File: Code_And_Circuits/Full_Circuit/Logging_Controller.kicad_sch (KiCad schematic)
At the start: 4 parts, among them J1 Micro_SD_Card_Slot, M1 GY-GPS6MV2

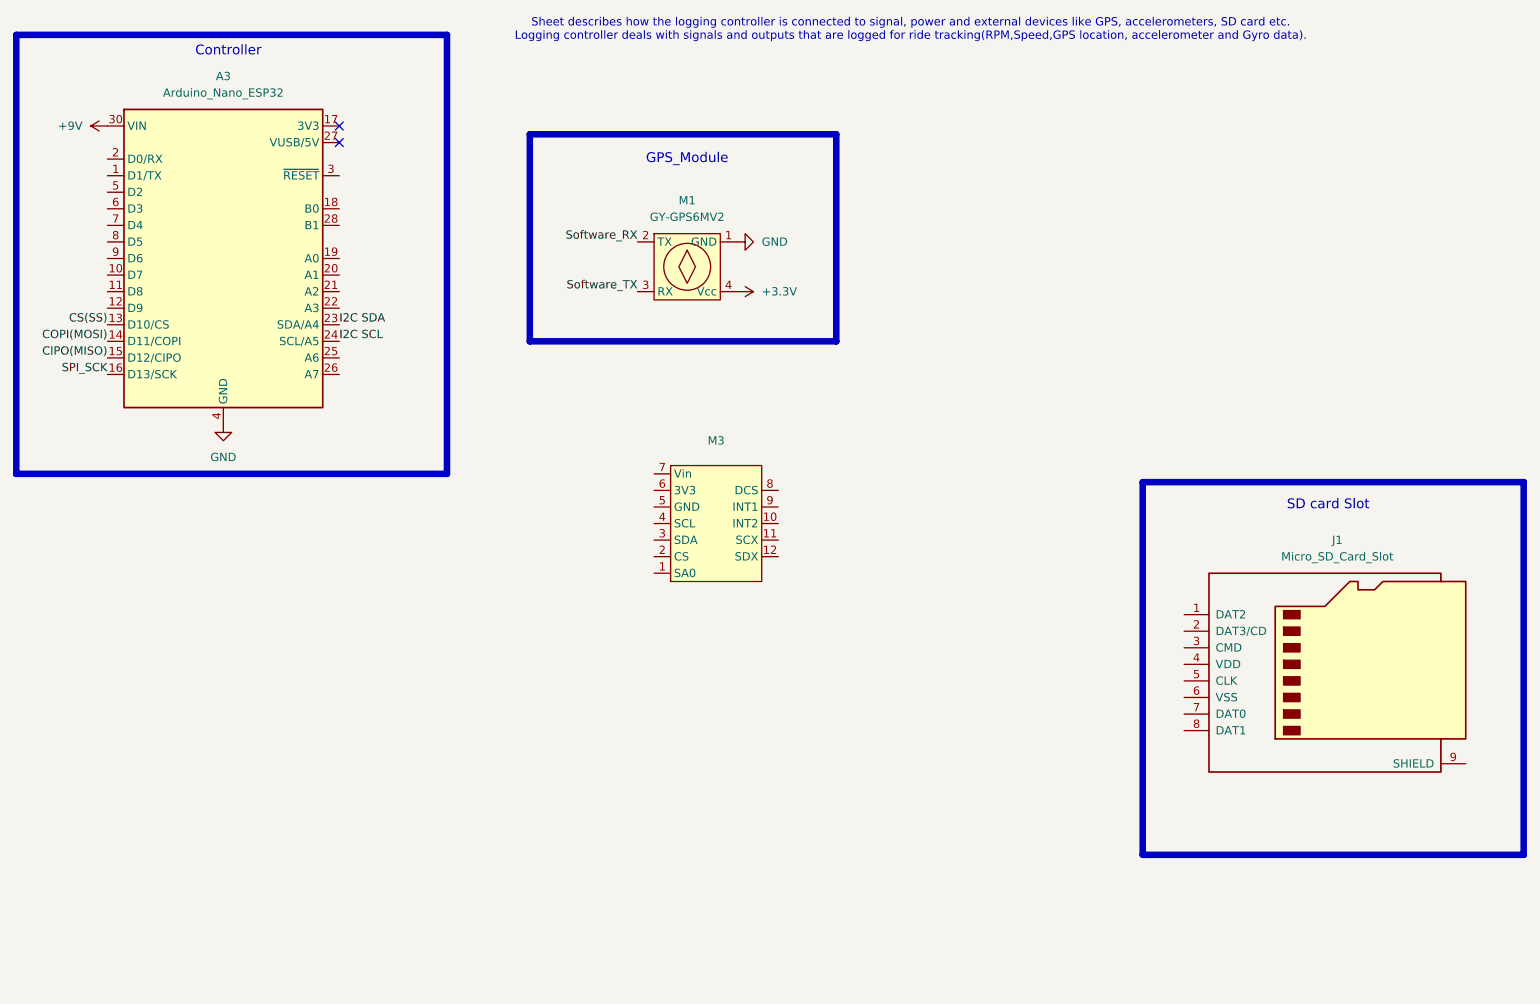
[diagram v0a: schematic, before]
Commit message: Finished schematic need to do PCB design and get Tachometer reference
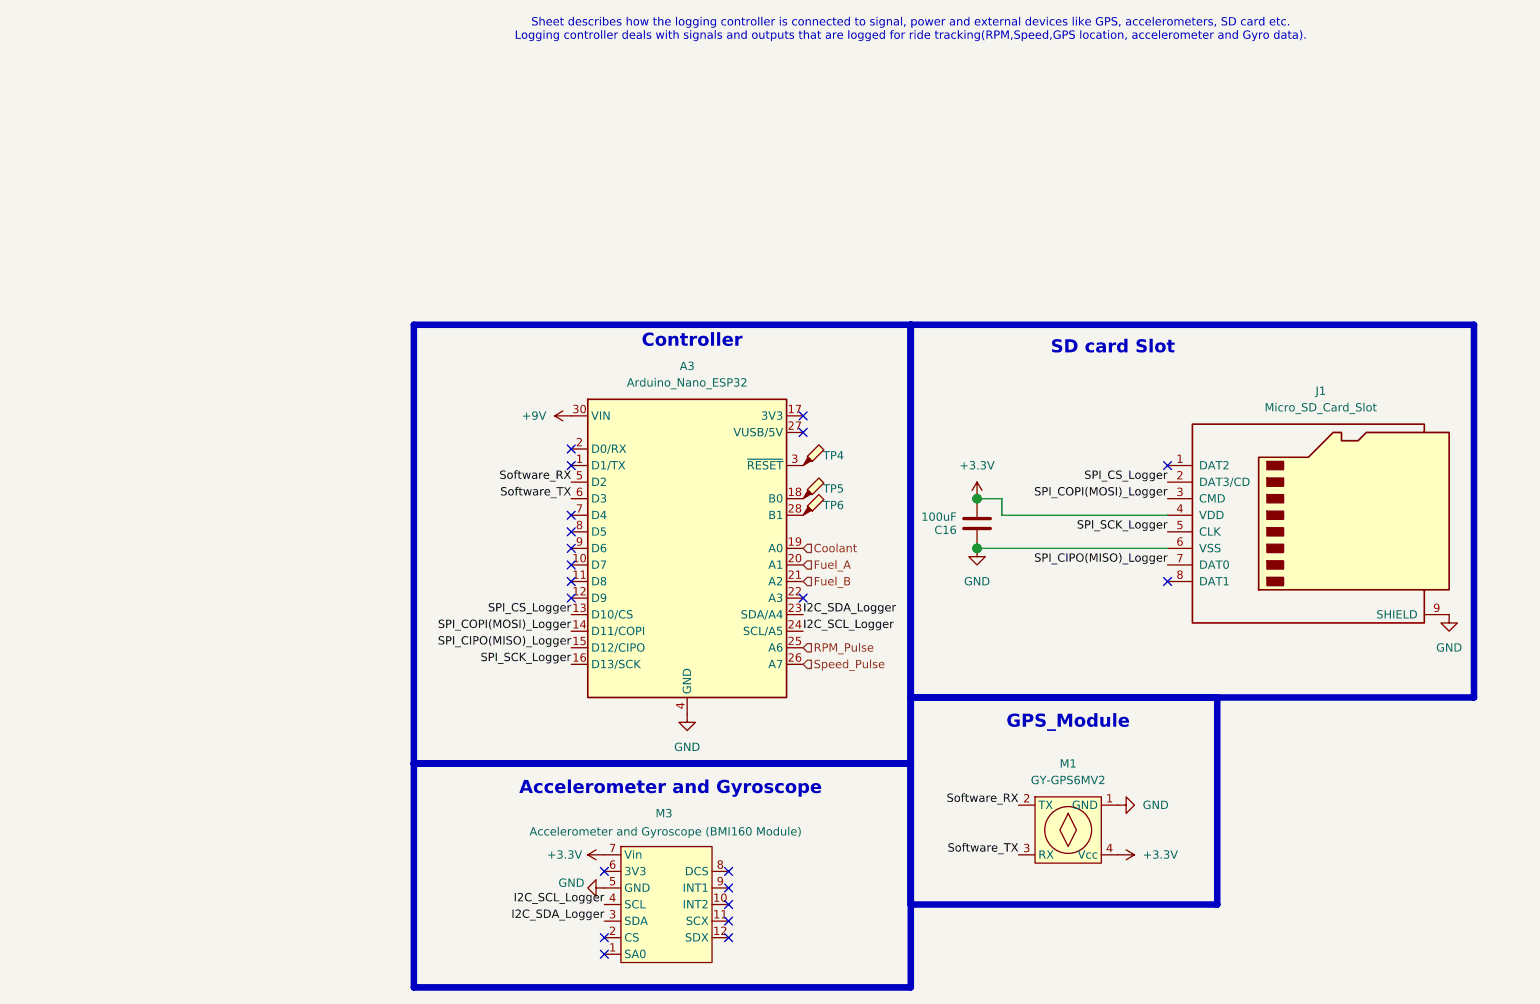
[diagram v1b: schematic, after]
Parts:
- added C16: 100uF, Capacitor_SMD:C_0805_2012Metric_Pad1.18x1.45mm_HandSolder, symbol Device:C
- added TP4, TP5, TP6: TestPoint, Connector_PinHeader_1.00mm:PinHeader_1x01_P1.00mm_Vertical, symbol Connector:TestPoint_Probe
- J1: footprint (none) -> Connector_Card:microSD_HC_Wuerth_693072010801
- M3: value ~ -> Accelerometer and Gyroscope (BMI160 Module)
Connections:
- net CIPO(MISO) is gone; now on net SPI_CIPO(MISO)_Logger: A3.15 (D12/CIPO)
- net COPI(MOSI) is gone; now on net SPI_COPI(MOSI)_Logger: A3.14 (D11/COPI)
- net CS(SS) is gone; now on net SPI_CS_Logger: A3.13 (D10/CS)
- net I2C SCL is gone; now on net I2C_SCL_Logger: A3.24 (SCL/A5)
- net I2C SDA is gone; now on net I2C_SDA_Logger: A3.23 (SDA/A4)
- net SPI_SCK is gone; now on net SPI_SCK_Logger: A3.16 (D13/SCK)
- net +3.3V: now also J1.4 (VDD), M3.7 (Vin), C16.2
- net GND: now also J1.6 (VSS), J1.9 (SHIELD), M3.5 (GND), C16.1
- net Software_RX: now also A3.5 (D2)
- net Software_TX: now also A3.6 (D3)
- net I2C_SDA_Logger: now reaches M3.3 (SDA)
- net I2C_SCL_Logger: now reaches M3.4 (SCL)
- net SPI_CS_Logger: now reaches J1.2 (DAT3/CD)
- net SPI_COPI(MOSI)_Logger: now reaches J1.3 (CMD)
- net SPI_SCK_Logger: now reaches J1.5 (CLK)
- net SPI_CIPO(MISO)_Logger: now reaches J1.7 (DAT0)
- net at A3.18 (B0): now also TP5.1
- net Coolant: now reaches A3.19 (A0)
- net Fuel_A: now reaches A3.20 (A1)
- net Fuel_B: now reaches A3.21 (A2)
- net RPM_Pulse: now reaches A3.25 (A6)
- net Speed_Pulse: now reaches A3.26 (A7)
- net at A3.28 (B1): now also TP6.1
- net at A3.3 (~{RESET}): now also TP4.1
- no-connect marks 2 -> 21
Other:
- note added: "Accelerometer and Gyroscope"
- moved on the sheet: A3, J1, M1, M3

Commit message: Reconfired some pin assignments for cleaner layout and adding reference footprints and mostly layed out board, due to space limits logging section has been ommitted
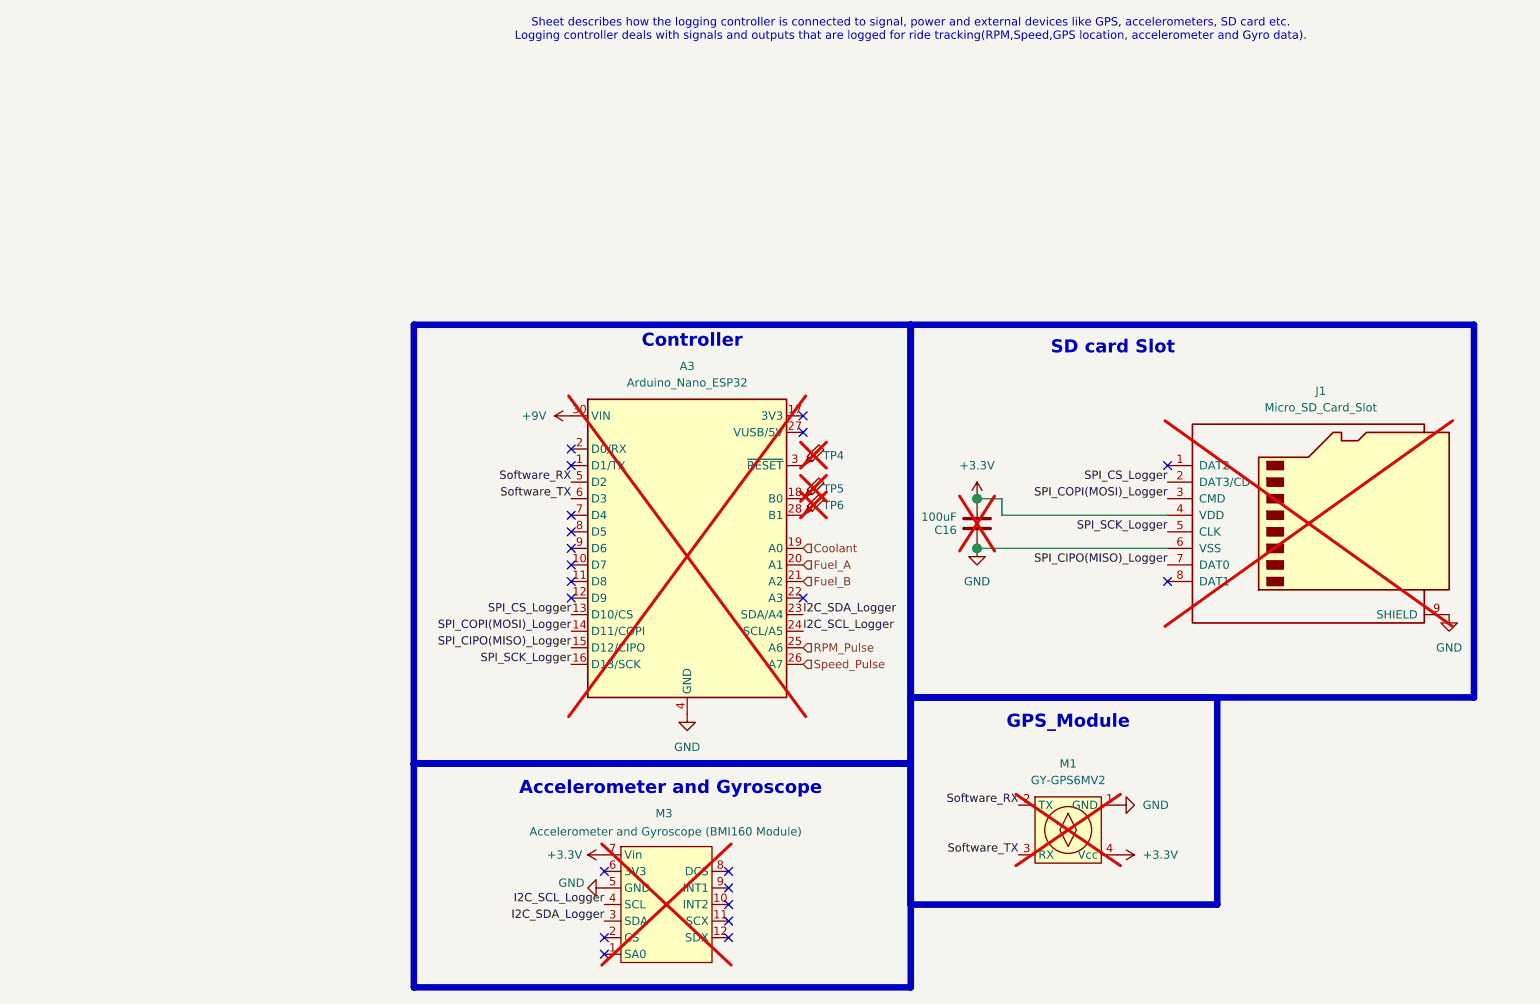
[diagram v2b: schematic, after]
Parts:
- A3, C16, J1, M1, TP4, TP5, TP6: now not fitted
- M3: footprint (none) -> Added_Footprints:BMI160_Module; now not fitted
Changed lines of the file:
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@@
 		(exclude_from_sim no)
 		(in_bom yes)
-		(on_board yes)
-		(dnp no)
+		(on_board no)
+		(dnp yes)
 		(property "Reference" "TP4"
 			(at 140.208 82.296 0)
@@
 		(exclude_from_sim no)
 		(in_bom yes)
-		(on_board yes)
-		(dnp no)
+		(on_board no)
+		(dnp yes)
 		(property "Reference" "TP6"
 			(at 140.208 89.916 0)
@@
 		(exclude_from_sim no)
 		(in_bom yes)
-		(on_board yes)
-		(dnp no)
+		(on_board no)
+		(dnp yes)
 		(property "Reference" "M3"
 			(at 115.824 137.16 0)
@@
 			)
 		)
-		(property "Footprint" ""
+		(property "Footprint" "Added_Footprints:BMI160_Module"
 			(at 115.57 151.13 0)
 			(effects
@@
 		(exclude_from_sim no)
 		(in_bom yes)
-		(on_board yes)
-		(dnp no)
+		(on_board no)
+		(dnp yes)
 		(fields_autoplaced yes)
 		(property "Reference" "J1"
@@
 		(exclude_from_sim no)
 		(in_bom yes)
-		(on_board yes)
-		(dnp no)
+		(on_board no)
+		(dnp yes)
 		(property "Reference" "C16"
 			(at 159.004 93.726 0)
@@
 		(exclude_from_sim no)
 		(in_bom yes)
-		(on_board yes)
-		(dnp no)
+		(on_board no)
+		(dnp yes)
 		(fields_autoplaced yes)
 		(property "Reference" "M1"
@@
 		(exclude_from_sim no)
 		(in_bom yes)
-		(on_board yes)
-		(dnp no)
+		(on_board no)
+		(dnp yes)
 		(property "Reference" "TP5"
 			(at 140.208 87.376 0)
@@
 		(exclude_from_sim no)
 		(in_bom yes)
-		(on_board yes)
-		(dnp no)
+		(on_board no)
+		(dnp yes)
 		(fields_autoplaced yes)
 		(property "Reference" "A3"
